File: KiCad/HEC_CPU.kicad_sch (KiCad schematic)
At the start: 20 parts, among them J3 Conn_02x05_Odd_Even, SW2 SW_Push, U1 Z80CPU, U16 74LS32, U18 74LS138, U20 74LS574, U21 74LS574, U22 74LS02, U23 74LS74, U34 74LS393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

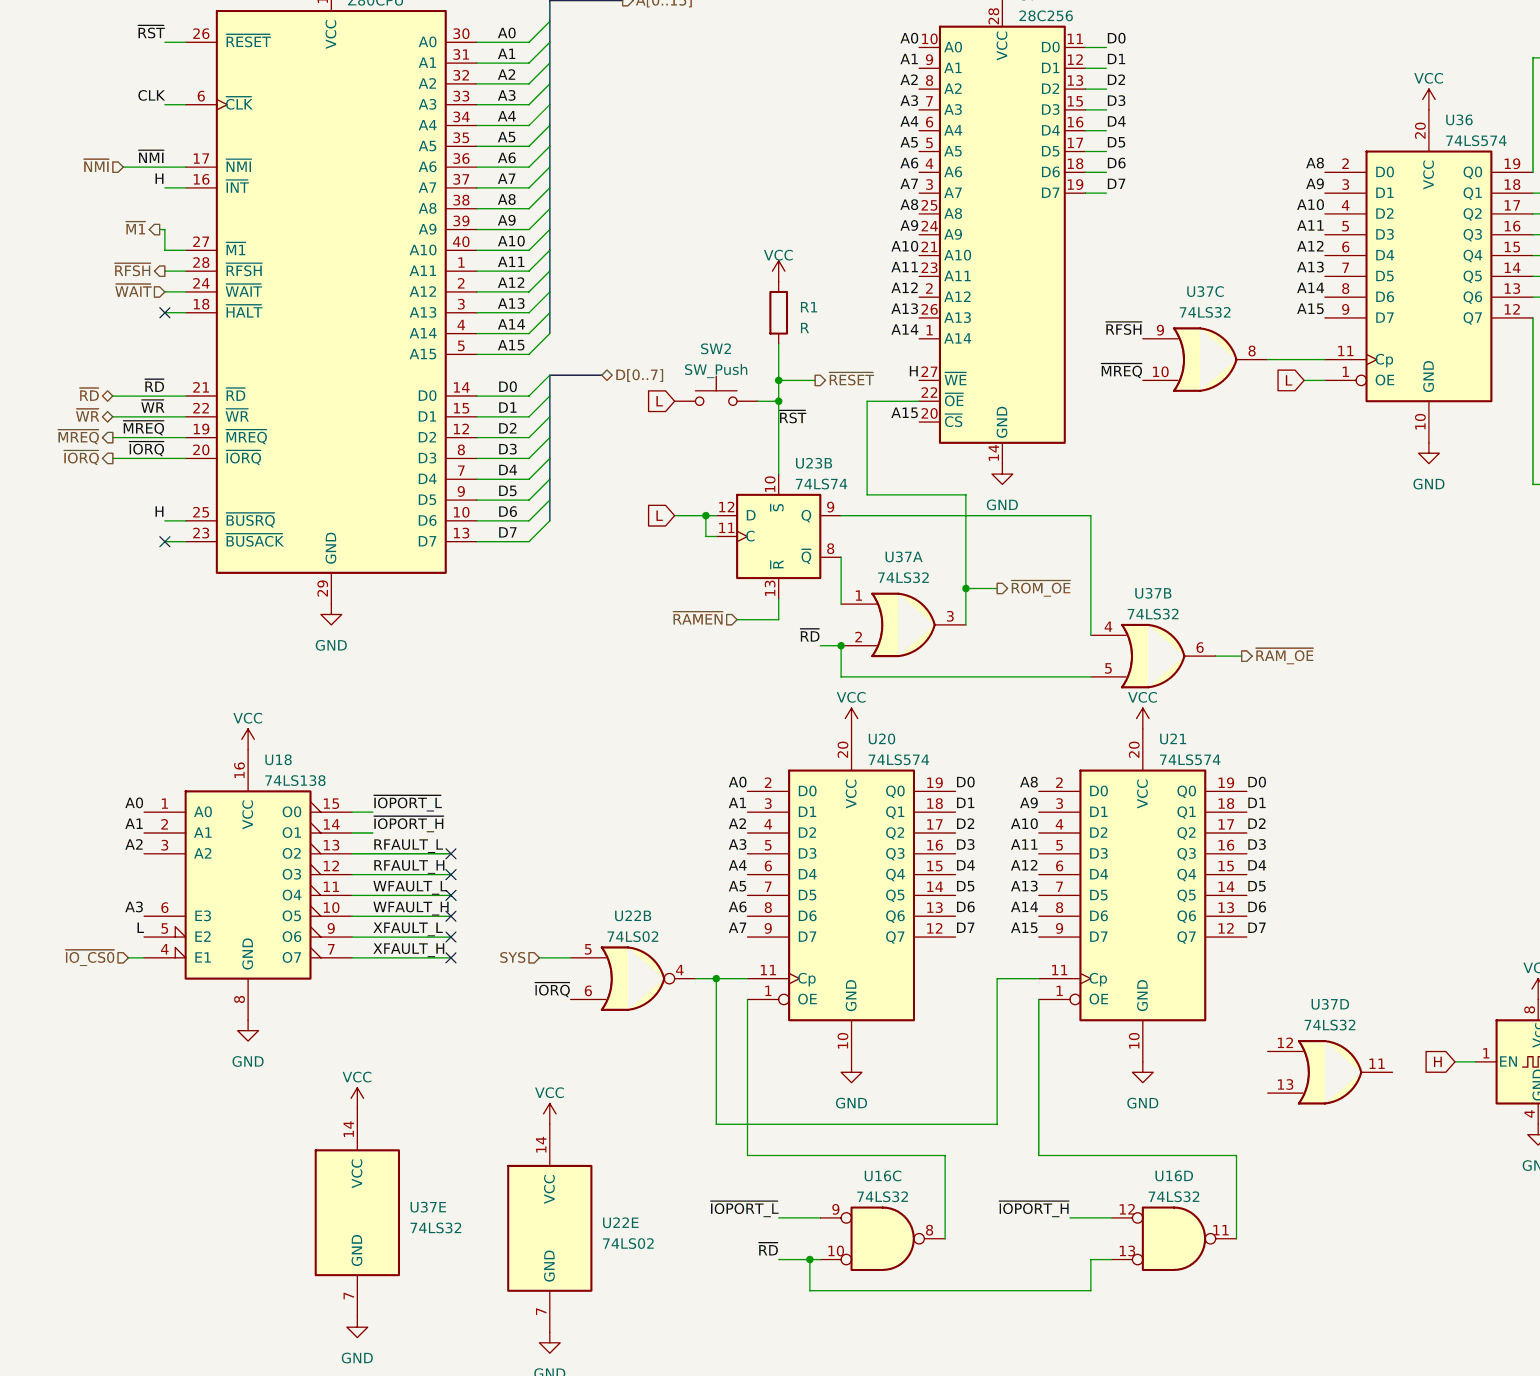
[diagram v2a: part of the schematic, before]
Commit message: Cleanup schematic
Cleanup the schematic for easier reading, reduce ERC errors.
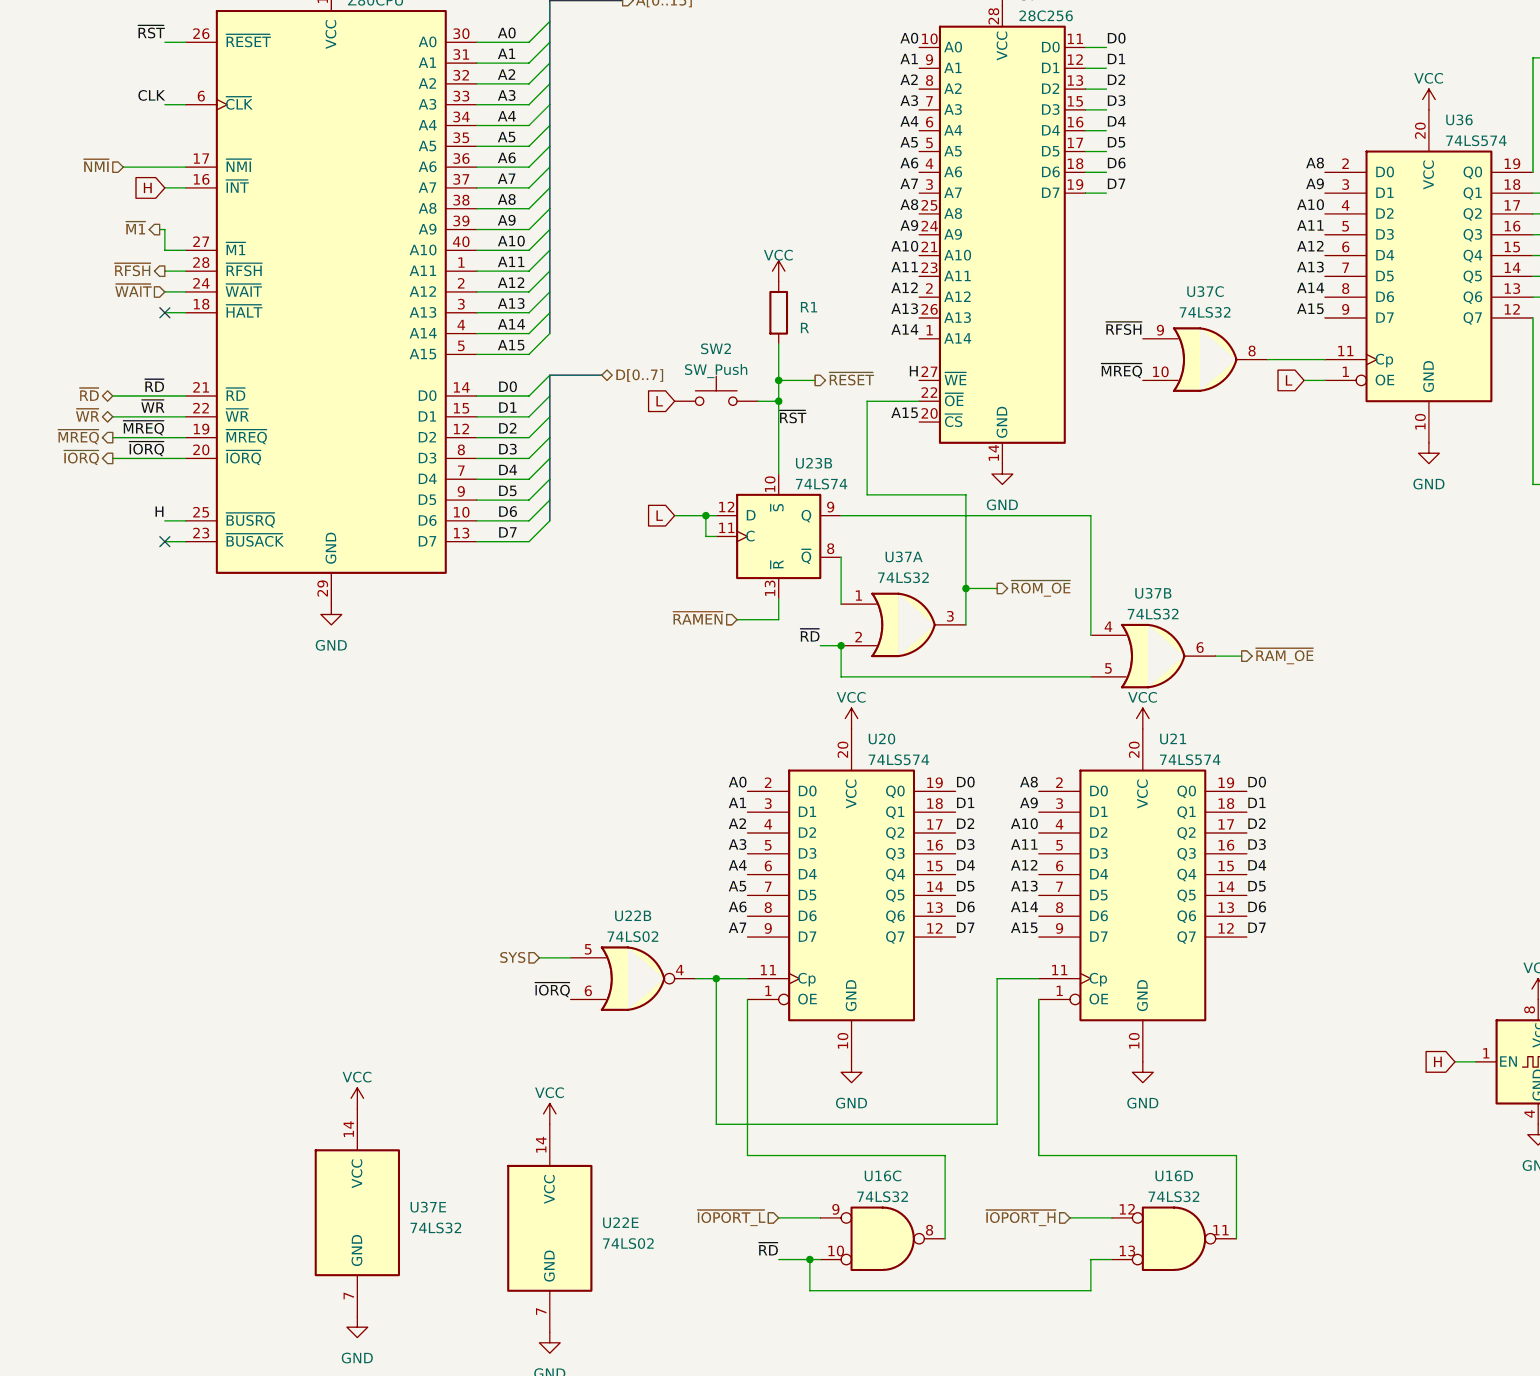
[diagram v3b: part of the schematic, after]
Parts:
- removed U18: 74LS138, Package_DIP:DIP-16_W7.62mm_Socket, symbol 74xx:74LS138
- removed unit 4 of U37
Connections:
- no-connect marks 10 -> 4

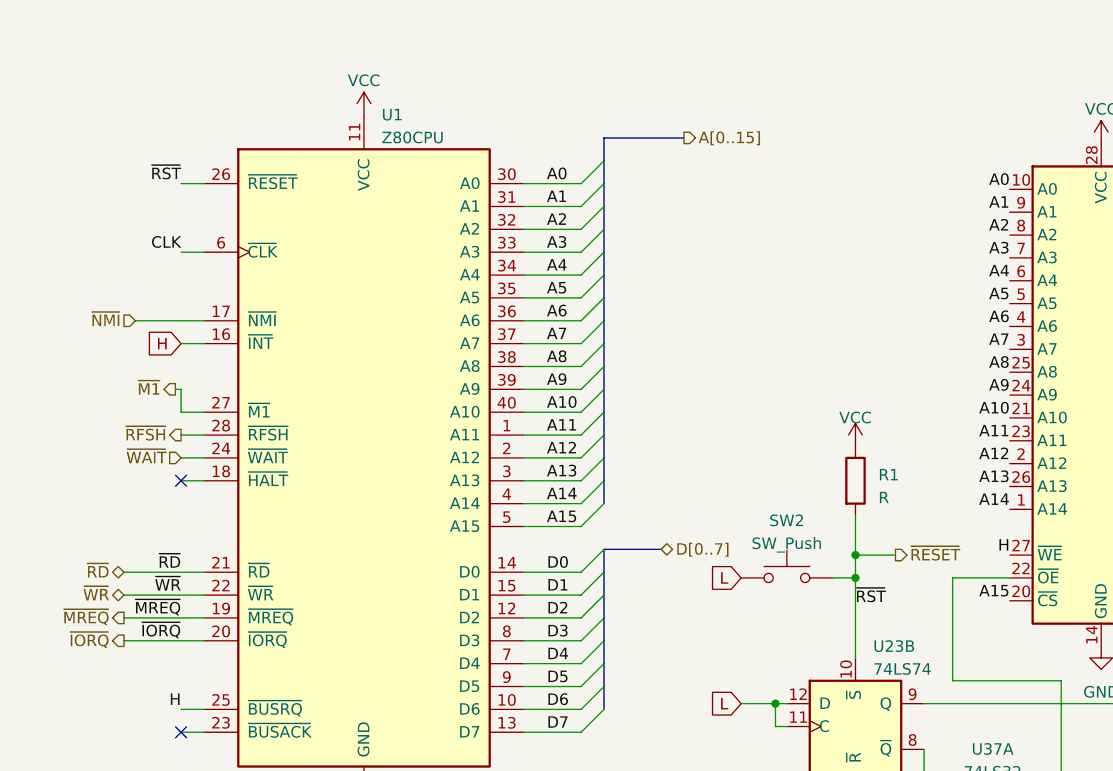
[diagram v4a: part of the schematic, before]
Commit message: Removed DMA from bus
Bus-mastering DMA has been removed from the expansion bus design due to complexity and bandwidth issue with external bus expansion circuit. The pins are replaced with audio output from on-bard sound system. Minor changes to pin names.
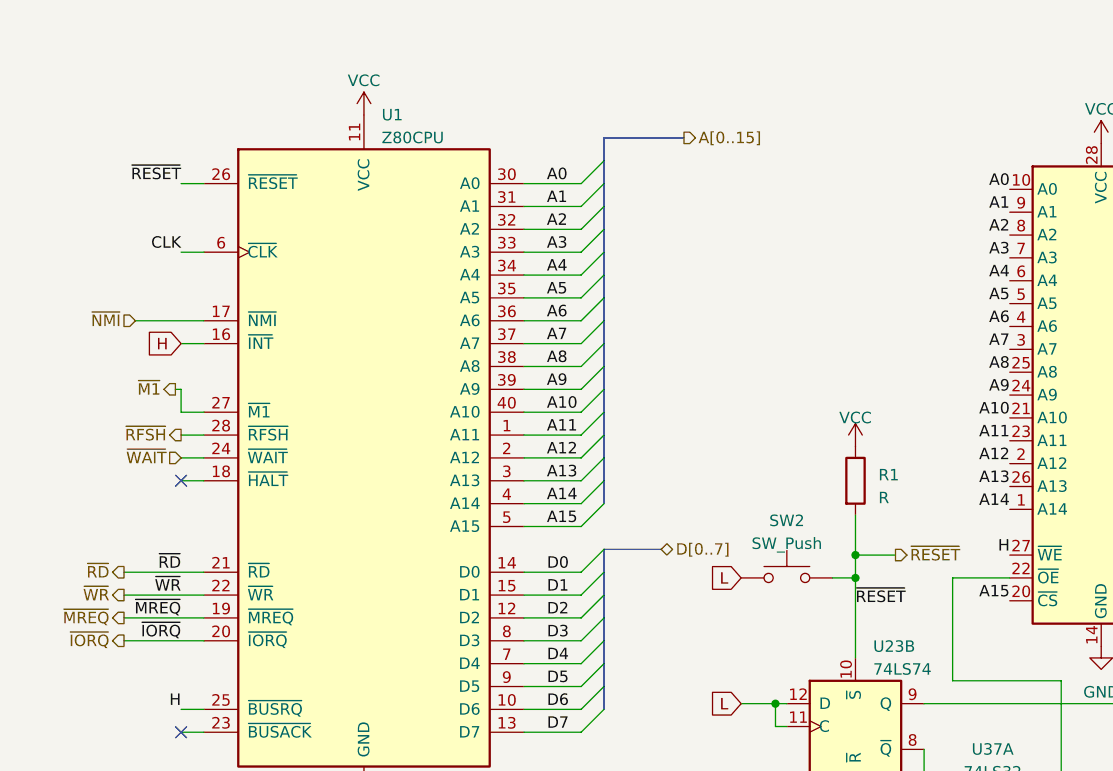
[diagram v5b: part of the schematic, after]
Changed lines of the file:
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@@
     (effects (font (size 1.27 1.27)) (justify right bottom))
   )
-  (label "~{RST}" (at 101.6 71.12 0) (fields_autoplaced)
+  (label "~{RESET}" (at 101.6 71.12 0) (fields_autoplaced)
     (effects (font (size 1.27 1.27)) (justify left bottom))
   )
@@
     (effects (font (size 1.27 1.27)) (justify right bottom))
   )
-  (label "~{RST}" (at 26.67 24.13 180) (fields_autoplaced)
+  (label "~{RESET}" (at 26.67 24.13 180) (fields_autoplaced)
     (effects (font (size 1.27 1.27)) (justify right bottom))
   )
@@
     (effects (font (size 1.27 1.27)) (justify right))
   )
-  (hierarchical_label "~{WR}" (shape tri_state) (at 20.32 69.85 180) (fields_autoplaced)
+  (hierarchical_label "~{WR}" (shape output) (at 20.32 69.85 180) (fields_autoplaced)
     (effects (font (size 1.27 1.27)) (justify right))
   )
@@
     (effects (font (size 1.27 1.27)) (justify right))
   )
-  (hierarchical_label "~{RD}" (shape tri_state) (at 20.32 67.31 180) (fields_autoplaced)
+  (hierarchical_label "~{RD}" (shape output) (at 20.32 67.31 180) (fields_autoplaced)
     (effects (font (size 1.27 1.27)) (justify right))
   )

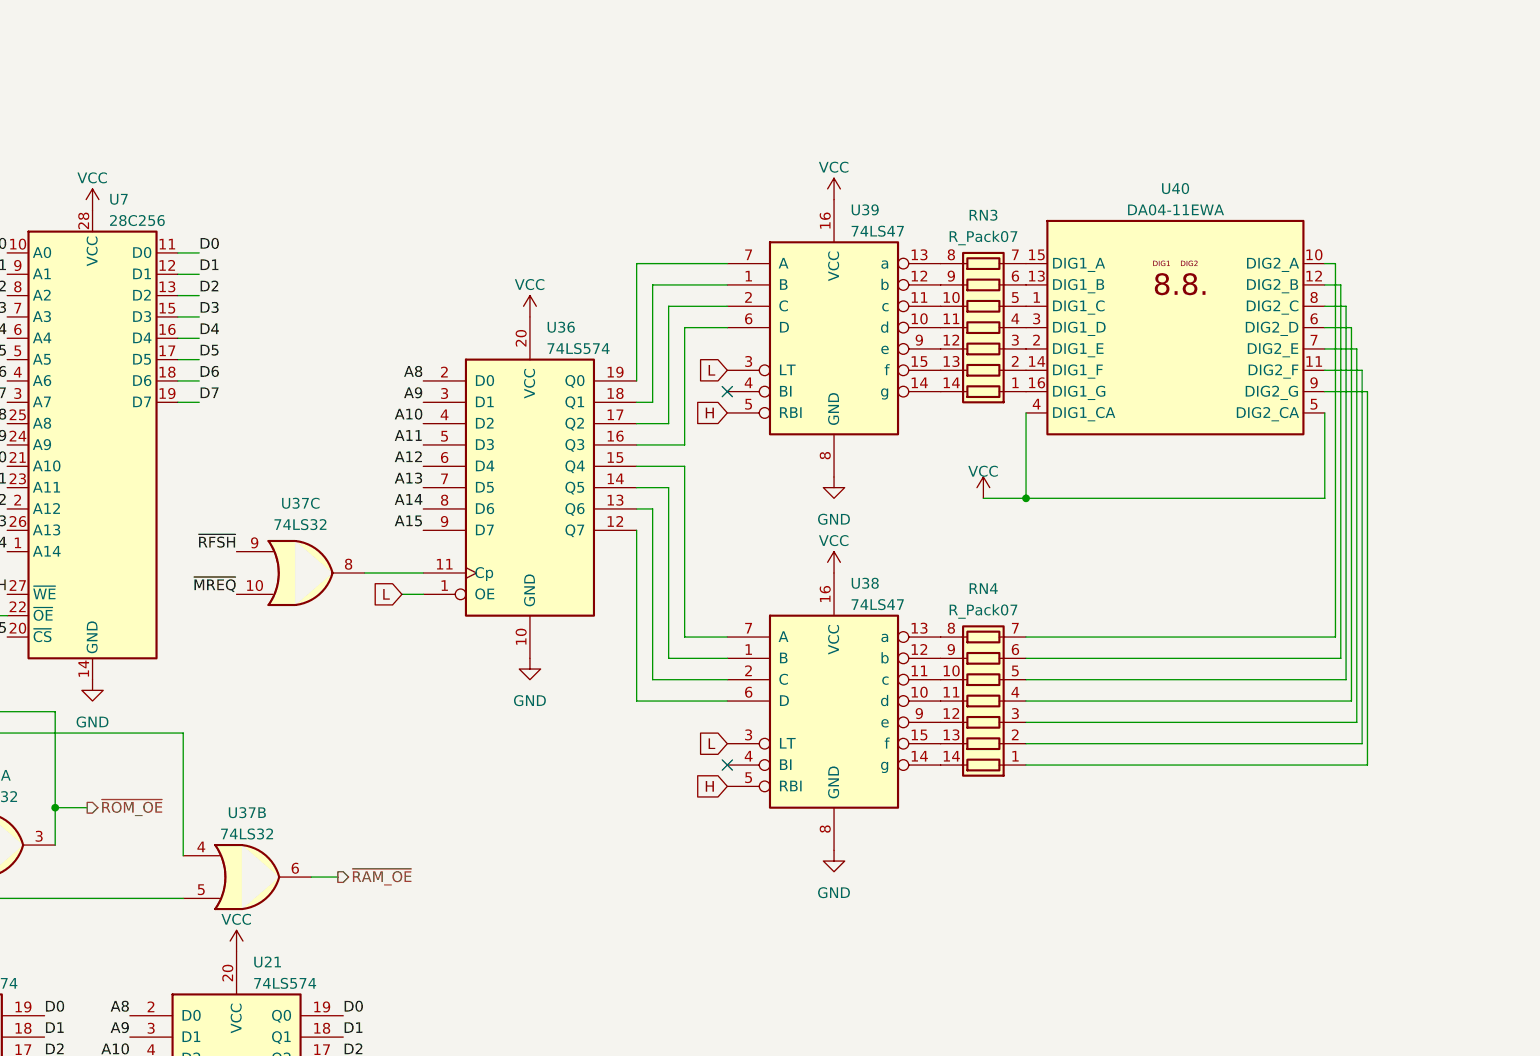
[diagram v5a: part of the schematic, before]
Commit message: PCB Layout attempt
Played with PCB layout a bit to get an idea of how the layout of HEC would look like. Minor updates to schematic to simplify  PCB layout.
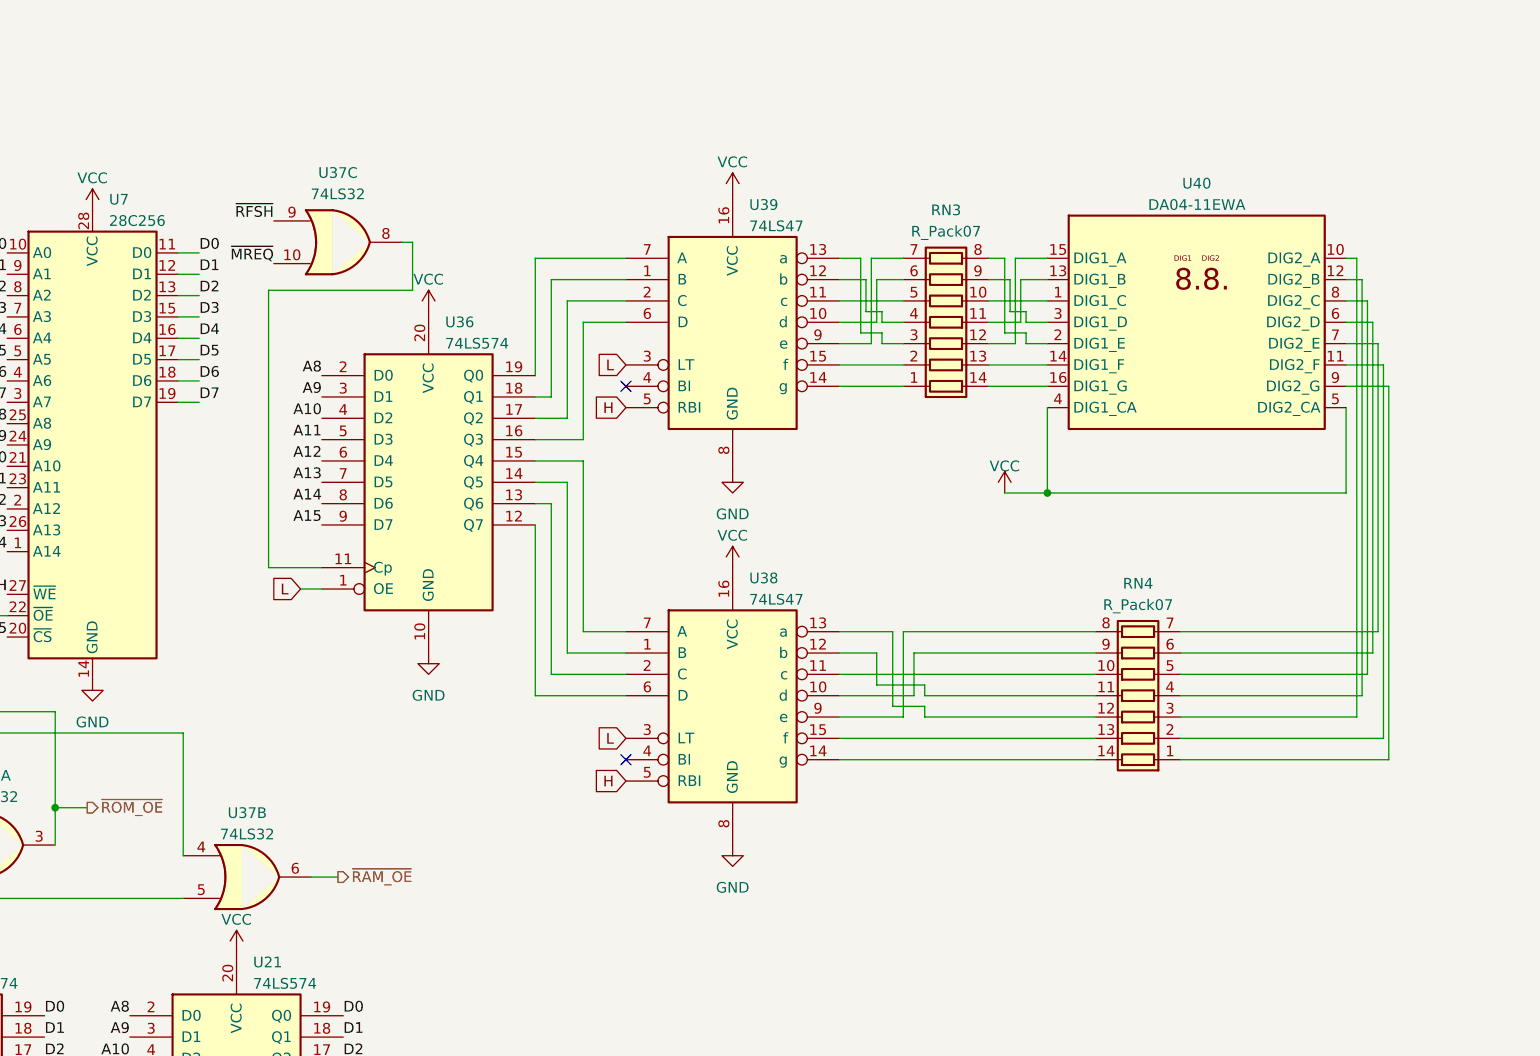
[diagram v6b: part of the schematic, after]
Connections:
- net at RN4.11 (R4.2): now also U38.12 (b); no longer U38.10 (d)
- net at RN4.12 (R3.2): now also U38.13 (a); no longer U38.9 (e)
- net at RN4.3 (R3.1): now also U40.10 (DIG2_A); no longer U40.7 (DIG2_E)
- net at RN4.4 (R4.1): now also U40.12 (DIG2_B); no longer U40.6 (DIG2_D)
- net at RN4.6 (R6.1): now also U40.6 (DIG2_D); no longer U40.12 (DIG2_B)
- net at RN4.7 (R7.1): now also U40.7 (DIG2_E); no longer U40.10 (DIG2_A)
- net at RN4.8 (R7.2): now also U38.9 (e); no longer U38.13 (a)
- net at RN4.9 (R6.2): now also U38.10 (d); no longer U38.12 (b)
- net at U40.1 (DIG1_C): now also RN3.10 (R5.2); no longer RN3.5 (R5.1)
- net at U40.13 (DIG1_B): now also RN3.11 (R4.2); no longer RN3.6 (R6.1)
- net at U40.14 (DIG1_F): now also RN3.13 (R2.2); no longer RN3.2 (R2.1)
- net at U40.15 (DIG1_A): now also RN3.12 (R3.2); no longer RN3.7 (R7.1)
- net at U40.16 (DIG1_G): now also RN3.14 (R1.2); no longer RN3.1 (R1.1)
- net at U40.2 (DIG1_E): now also RN3.8 (R7.2); no longer RN3.3 (R3.1)
- net at U40.3 (DIG1_D): now also RN3.9 (R6.2); no longer RN3.4 (R4.1)
- net at U39.11 (c): now also RN3.5 (R5.1); no longer RN3.10 (R5.2)
- net at U39.10 (d): now also RN3.6 (R6.1); no longer RN3.11 (R4.2)
- net at U39.9 (e): now also RN3.7 (R7.1); no longer RN3.12 (R3.2)
- net at U39.15 (f): now also RN3.2 (R2.1); no longer RN3.13 (R2.2)
- net at U39.14 (g): now also RN3.1 (R1.1); no longer RN3.14 (R1.2)
- net at U39.13 (a): now also RN3.3 (R3.1); no longer RN3.8 (R7.2)
- net at U39.12 (b): now also RN3.4 (R4.1); no longer RN3.9 (R6.2)
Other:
- moved on the sheet: RN3, RN4, U36, U37C, U38, U39, U40
